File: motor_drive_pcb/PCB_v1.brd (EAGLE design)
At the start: 120.7 x 57.2 mm, 44 parts, among them IC1 MCP604P, J1 FRDM-K64F

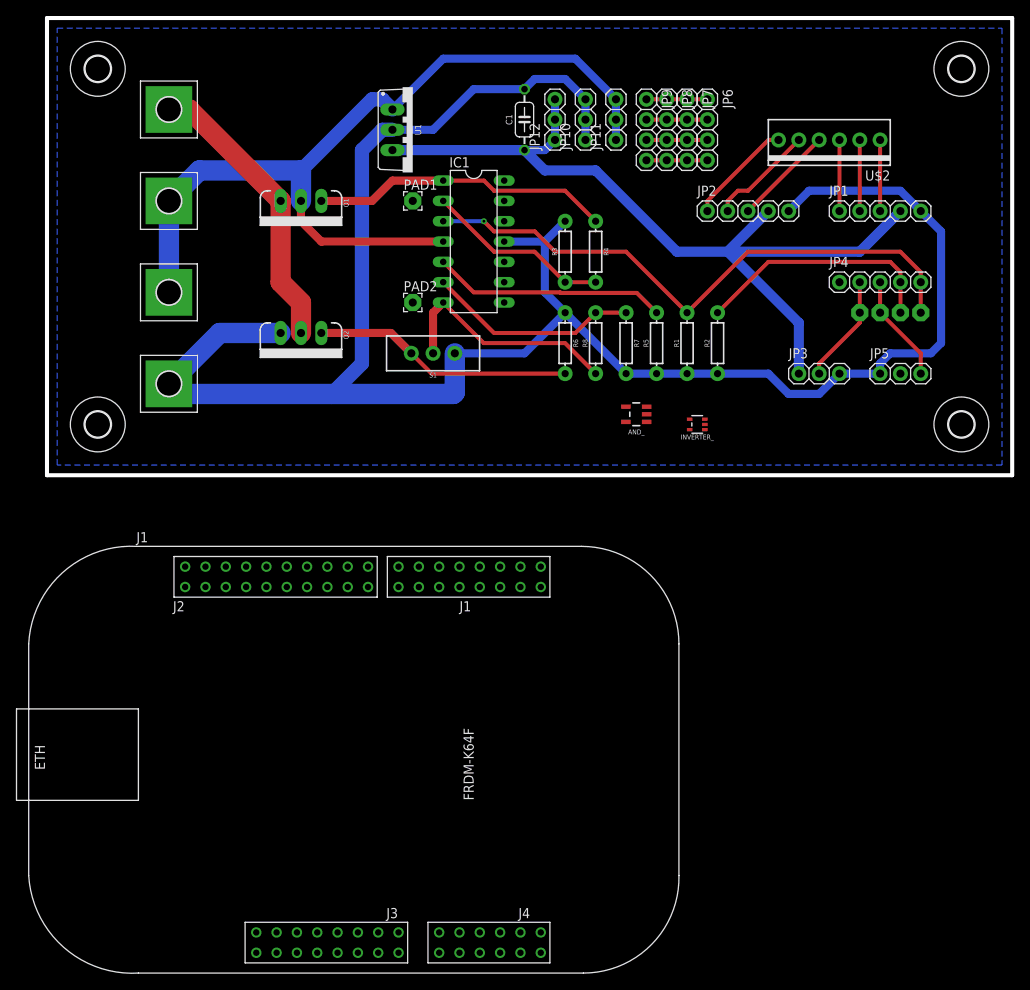
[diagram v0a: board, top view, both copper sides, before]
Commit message: updated pcb and encoder schematics and boards
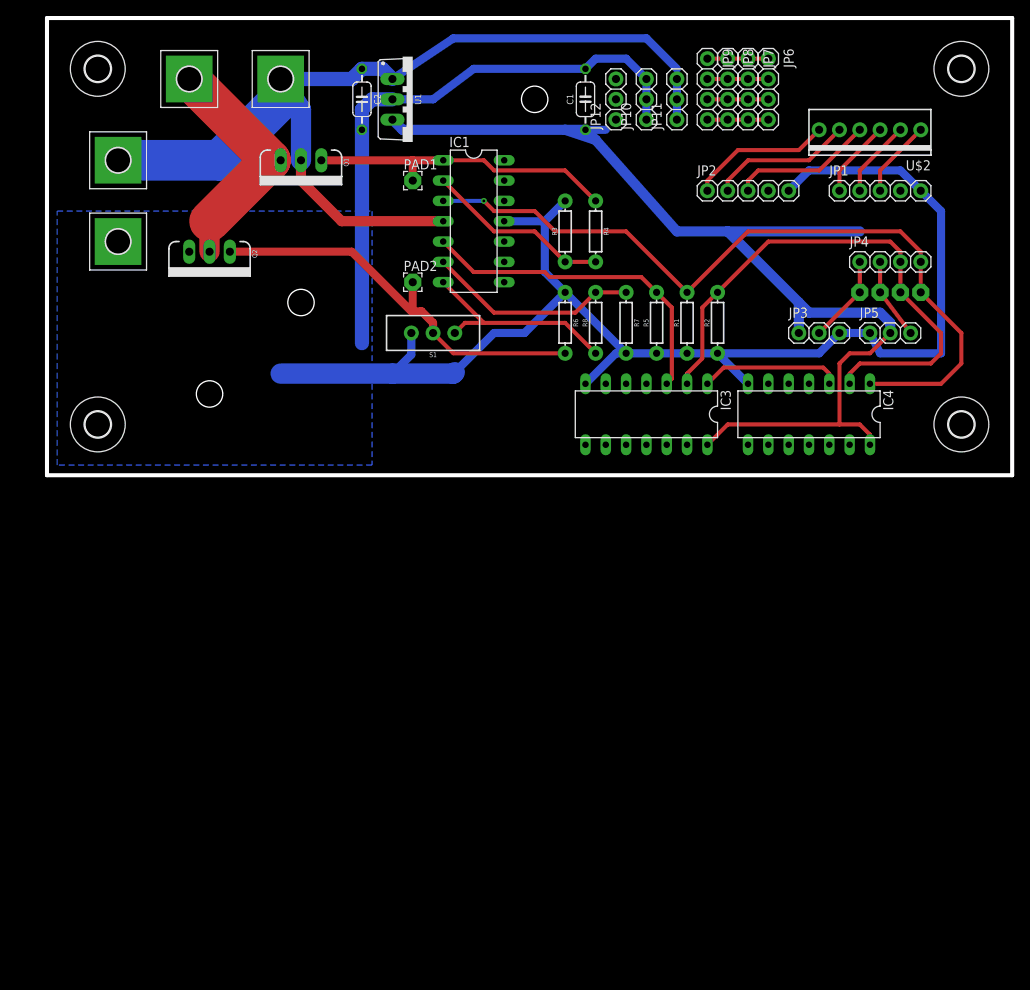
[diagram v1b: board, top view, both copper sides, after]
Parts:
- removed AND_: (no value), SparkFun-IC-Logic:SOT23-5
- removed INVERTER_: (no value), SparkFun-IC-Logic:SOT353
- removed J1: FRDM-K64F, ee192:FRDM-K64F
- added C2: (no value), bt_rcl:C075
- added IC3: 4081N, 40xx:DIL14
- added IC4: 4030N, 40xx:DIL14
- JP4: device ee192:1X05 -> ee192:1X04
- moved BATT+1 20.7 mm to (-17.8, 45.7)
- moved BATT- 18.9 mm to (-38.1, 25.4)
- moved BATT+ 17.7 mm to (-38.1, 35.6)
- moved Q2 15.3 mm to (-26.7, 24.1)
- moved JP8 9.16 mm to (38.1, 44.5)
- moved JP9 9.16 mm to (35.6, 44.5)
- moved JP6 9.16 mm to (43.2, 44.5)
- moved JP7 9.16 mm to (40.6, 44.5)
- moved C1 8.03 mm to (20.3, 43.2)
- moved JP10 8.03 mm to (27.9, 43.2)
- moved JP11 8.03 mm to (31.8, 43.2)
- moved JP12 8.03 mm to (24.1, 43.2)
- moved U$2 5.24 mm to (55.9, 39.4)
- moved JP5 5.24 mm to (58.4, 14.0)
- moved Q1 5.08 mm to (-15.2, 35.6)
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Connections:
- removed net 3.3V: AND_.5, INVERTER_.5, JP4.1
- removed net N$4: AND_.4, IC1.5, R5.P$2
- net GND: now also C2.2, IC3.7, IC4.7, S1.1; no longer AND_.3, INVERTER_.3, J1.J2-3, S1.3
- net N$15: now also JP4.2; no longer JP4.3
- net N$16: now also IC4.1, JP4.4; no longer INVERTER_.2, JP4.5
- net N$17: now also IC3.2, IC4.2, JP4.3; no longer AND_.2, JP4.4
- net N$18: now also IC3.14, IC4.14, JP5.2
- net N$19: now also JP4.1; no longer JP4.2
- net N$20: now also IC1.5, IC3.3, R5.P$2; no longer JP5.2
- net N$5: now also S1.2; no longer S1.1
- net N$7: now also S1.3; no longer S1.2
- net N$8: now also IC3.1, IC4.3; no longer AND_.1, INVERTER_.4
- net V_BATT: now also C2.1
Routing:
- net N$20: track 0.00 -> 41.8 mm
- net N$17: track 31.1 -> 67.6 mm
- net N$18: track 106.4 -> 140.0 mm
- net N$4: track 29.3 -> 0.00 mm
- net N$16: track 73.7 -> 97.2 mm
- net N$5: track 32.6 -> 51.5 mm
- net N$8: track 0.00 -> 17.7 mm
- net V_BATT: track 108.5 -> 119.4 mm
- net GND: track 252.9 -> 242.5 mm
- net N$6: track 36.3 -> 27.7 mm
- net N$11: track 12.6 -> 17.9 mm
- net N$9: track 13.3 -> 17.9 mm
- net N$10: track 13.3 -> 17.9 mm
- net N$15: track 13.5 -> 10.2 mm
- net N$7: track 29.6 -> 26.9 mm
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- added copper zone on layer 16, net GND
- removed copper zone on layer 16, net N$21
